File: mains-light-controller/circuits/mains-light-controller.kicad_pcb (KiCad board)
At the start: 2 copper layers, 100 x 100 mm, 20 parts, among them J1 Screw_Terminal_01x03, J2 Screw_Terminal_01x02, Q1 BT136-500, SW1 SW_Push, U1 LTV-817, U2 HLK-PM05, U3 MOC3021M, U4 WeMos_mini

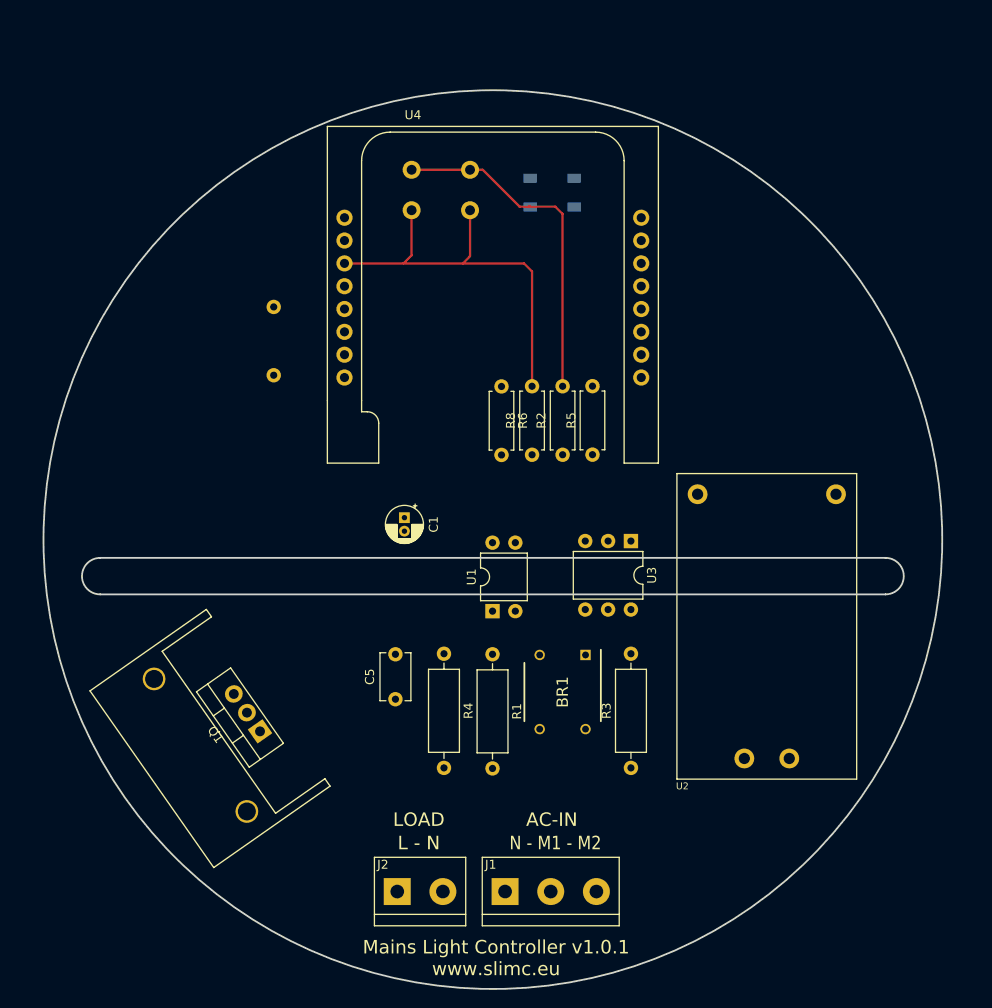
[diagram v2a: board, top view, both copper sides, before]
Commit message: new PCB layout and traces for mains light controller
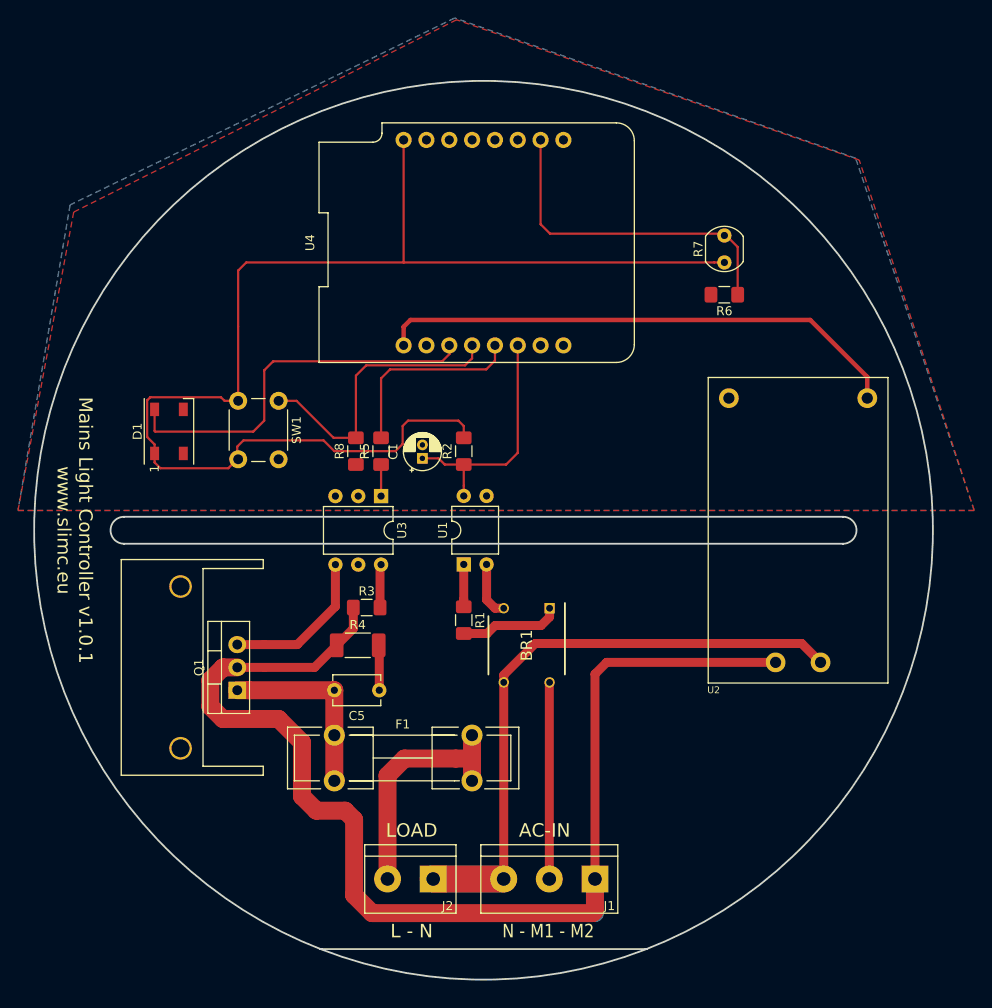
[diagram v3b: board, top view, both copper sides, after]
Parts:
- added F1: Fuse, Fuse_Holders_and_Fuses:Fuseholder5x20_horiz_open_lateral_Type-II, F.Cu at (48.4, 87.8)
- D1, SW1: moved to F.Cu
- R1, R3: footprint Resistor_THT:R_Axial_DIN0309_L9.0mm_D3.2mm_P12.70mm_Horizontal -> Resistor_SMD:R_1206_3216Metric_Pad1.42x1.75mm_HandSolder
- R2, R5, R6, R8: footprint Resistor_THT:R_Axial_DIN0207_L6.3mm_D2.5mm_P7.62mm_Horizontal -> Resistor_SMD:R_1206_3216Metric_Pad1.42x1.75mm_HandSolder
- R4: footprint Resistor_THT:R_Axial_DIN0309_L9.0mm_D3.2mm_P12.70mm_Horizontal -> Resistor_SMD:R_2010_5025Metric_Pad1.52x2.65mm_HandSolder
- R7: footprint OptoDevice:R_LDR_10x8.5mm_P7.6mm_Vertical -> OptoDevice:R_LDR_5.0x4.1mm_P3mm_Vertical; moved to F.Cu
- U4: footprint wemos-d1-mini:wemos-d1-mini-embedded -> wemos-d1-mini:wemos-d1-mini-connectors-only
- moved R7 51.7 mm to (91.8, 35.2)
- moved D1 50.2 mm to (30.0, 54.0), turned to 90 degrees
- moved R3 34.4 mm to (52.0, 73.6), turned to 0 degrees
- moved SW1 33.4 mm to (42.2, 50.6), turned to 270 degrees
- moved U3 28.2 mm to (53.6, 61.2)
- moved R6 26.8 mm to (91.8, 38.8), turned to 180 degrees
- moved R5 23.5 mm to (53.6, 56.2)
- moved R8 19.6 mm to (50.8, 56.2)
- moved U2 11.2 mm to (100.0, 65.0)
- moved R2 11.0 mm to (62.8, 56.2)
- moved J1 10.1 mm to (77.4, 103.8), turned to 180 degrees
- moved R4 9.65 mm to (51.0, 77.8), turned to 0 degrees
- moved C1 6.90 mm to (58.2, 57.0), turned to 90 degrees
- moved BR1 6.56 mm to (69.8, 77.8)
- moved U4 6.20 mm to (65.0, 33.0), turned to 0 degrees
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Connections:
- C1 pad 1: D8 -> D1
- D1 pad 4: D1 -> D4
- J1 pad 1: N_MAIN -> M2_IN
- J1 pad 3: M2_IN -> N_MAIN
- J2 pad 1: L_OUT -> N_MAIN
- J2 pad 2: N_MAIN -> Net-(F1-Pad2)
- R2 pad 1: D8 -> D1
- R5 pad 2: D3 -> D2
- R8 pad 2: D0 -> D3
- SW1 pad 1: +3V3 -> D3
- SW1 pad 2: D0 -> +3V3
- U1 pad 4: D8 -> D1
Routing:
- net M2_IN: track 0.00 -> 135.2 mm
- net +3V3: track 38.2 -> 141.6 mm
- net N_MAIN: track 0.00 -> 76.0 mm
- net +5V: track 0.00 -> 59.0 mm
- net D0: track 46.6 -> 0.00 mm
- net D4: track 0.00 -> 43.1 mm
- net A0: track 0.00 -> 37.7 mm
- net D3: track 0.00 -> 32.5 mm
- net Net-(F1-Pad2): track 0.00 -> 26.9 mm
- net D1: track 0.00 -> 26.9 mm
- net M1_IN: track 0.00 -> 21.9 mm
- net D2: track 0.00 -> 21.8 mm
- net L_OUT: track 0.00 -> 20.9 mm
- net Net-(Q1-Pad3): track 0.00 -> 17.4 mm
- net Net-(BR1-Pad1): track 0.00 -> 11.3 mm
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- added copper zone on B.Cu, net GND
- added copper zone on F.Cu, net GND
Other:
- outline, holes or cut-outs redrawn

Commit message: gerbers export
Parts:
- moved R2 8.82 mm to (54.0, 56.2)
- moved C1 4.66 mm to (62.9, 57.0)
- moved R5 2.54 mm to (51.1, 56.2)
- moved R8 2.54 mm to (48.3, 56.2)
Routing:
- net M2_IN: track 135.2 -> 204.0 mm
- net Net-(F1-Pad2): track 26.9 -> 52.9 mm
- net L_OUT: track 20.9 -> 41.8 mm
- net D1: track 26.9 -> 34.8 mm
- net +3V3: track 141.6 -> 134.2 mm
- net D3: track 32.5 -> 35.6 mm
- net Net-(R5-Pad1): track 3.51 -> 4.56 mm
- net D2: track 21.8 -> 22.8 mm
